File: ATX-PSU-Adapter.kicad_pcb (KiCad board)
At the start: 2 copper layers, 65 x 45 mm, 13 parts, among them J1 Conn_02x12_Top_Bottom, J2 Conn_01x06, J3 Conn_01x06, J4 Conn_01x06, J5 Conn_01x06, J6 Conn_01x06, J7 Conn_02x03_Odd_Even, U1 PC817

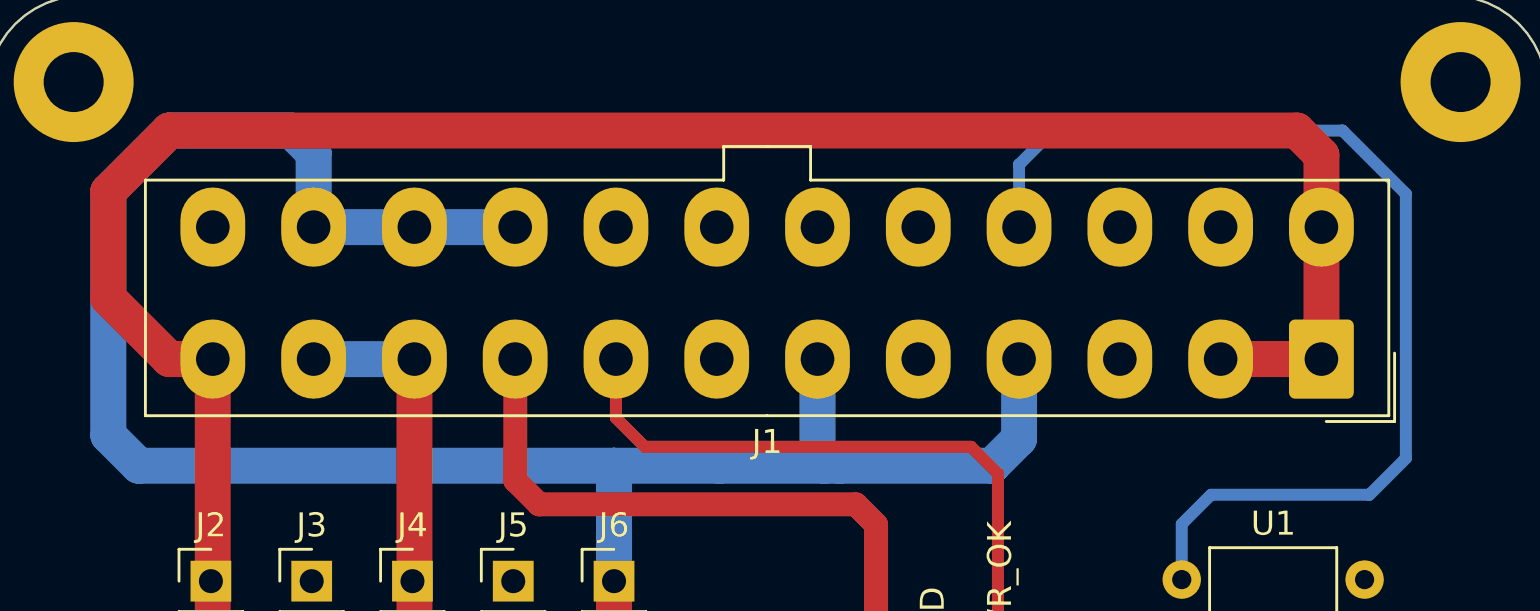
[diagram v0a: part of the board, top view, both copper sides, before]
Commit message: Replace ATX Connector
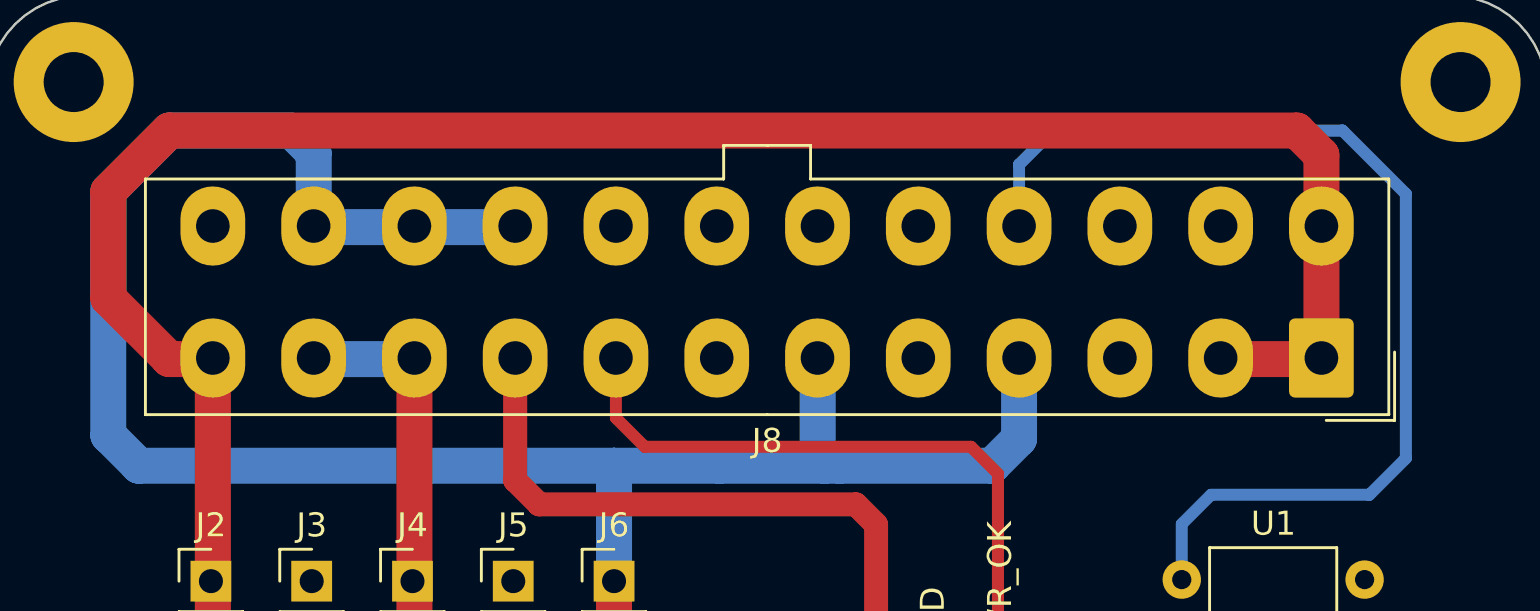
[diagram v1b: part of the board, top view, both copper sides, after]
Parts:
- removed J1: Conn_02x12_Top_Bottom, Connector_Molex:Molex_Mini-Fit_Jr_5566-24A_2x12_P4.20mm_Vertical
- added J8: ATX-24, Connector_Molex:Molex_Mini-Fit_Jr_5566-24A_2x12_P4.20mm_Vertical, F.Cu at (80.6, 40.1)
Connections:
- net +12V renamed /12V
- net +3.3V renamed /3.3V
- net +5P renamed /5VSB
- net +5V renamed /5V
- net /RPI-PS-ON renamed Net-(J7-Pin_5)
- J7 pad 6: /PG -> /PWR_OK
- U1 pad 3: /PS-ON -> /PS_ON
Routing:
- net /PS_ON: track 0.00 -> 44.2 mm
- net /PS-ON: track 44.2 -> 0.00 mm
- net /PWR_OK: track 0.00 -> 29.0 mm
- net /PG: track 29.0 -> 0.00 mm

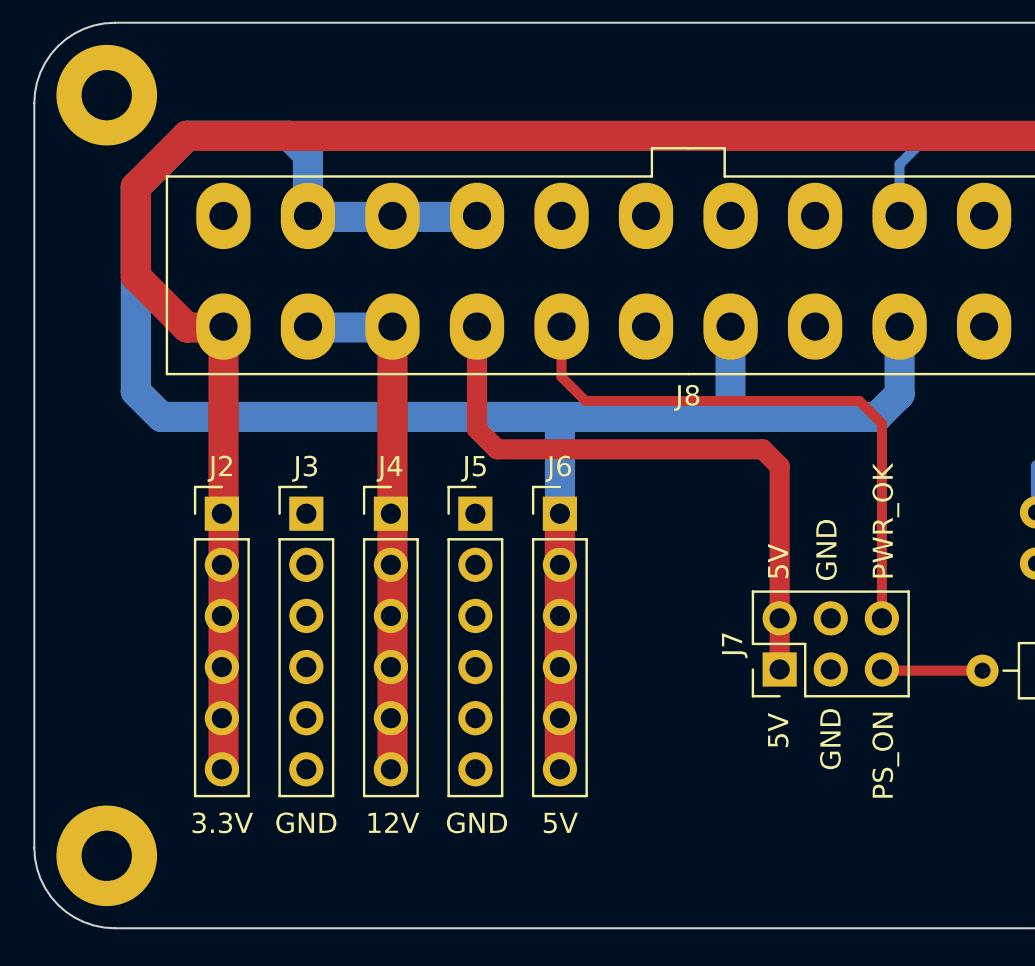
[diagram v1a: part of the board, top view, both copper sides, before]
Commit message: Replace pinheader
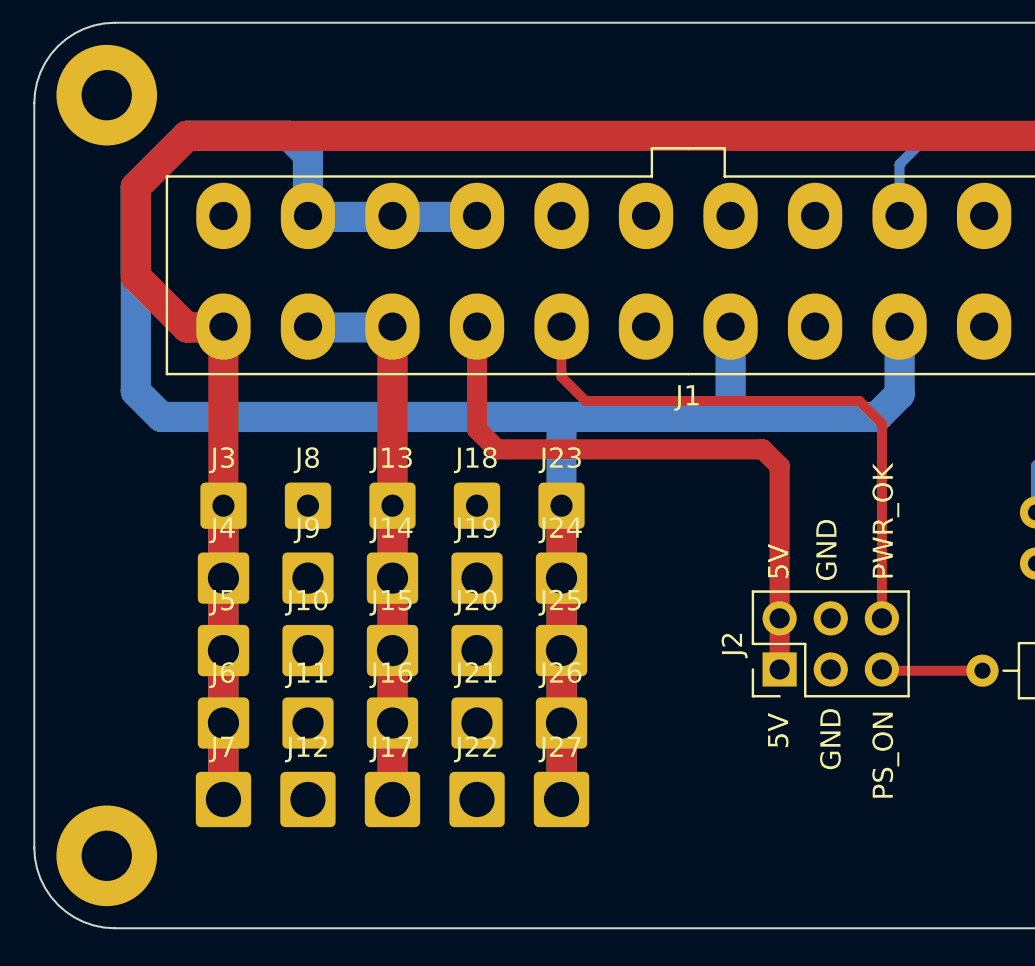
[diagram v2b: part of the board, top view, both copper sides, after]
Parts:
- removed the J2 at (34.3, 49.4)
- added J10: Conn_01x01, Connector_Wire:SolderWire-0.75sqmm_1x01_D1.25mm_OD2.3mm, F.Cu at (38.6, 56.2)
- added J11: Conn_01x01, Connector_Wire:SolderWire-0.75sqmm_1x01_D1.25mm_OD2.3mm, F.Cu at (38.6, 59.8)
- added J12: Conn_01x01, Connector_Wire:SolderWire-1sqmm_1x01_D1.4mm_OD2.7mm, F.Cu at (38.6, 63.6)
- added J13: Conn_01x01, Connector_Wire:SolderWire-0.5sqmm_1x01_D0.9mm_OD2.3mm, F.Cu at (42.8, 49.0)
- added J14: Conn_01x01, Connector_Wire:SolderWire-0.75sqmm_1x01_D1.25mm_OD2.3mm, F.Cu at (42.8, 52.6)
- added J15: Conn_01x01, Connector_Wire:SolderWire-0.75sqmm_1x01_D1.25mm_OD2.3mm, F.Cu at (42.8, 56.2)
- added J16: Conn_01x01, Connector_Wire:SolderWire-0.75sqmm_1x01_D1.25mm_OD2.3mm, F.Cu at (42.8, 59.8)
- added J17: Conn_01x01, Connector_Wire:SolderWire-1sqmm_1x01_D1.4mm_OD2.7mm, F.Cu at (42.8, 63.6)
- added J18: Conn_01x01, Connector_Wire:SolderWire-0.5sqmm_1x01_D0.9mm_OD2.3mm, F.Cu at (47.0, 49.0)
- added J19: Conn_01x01, Connector_Wire:SolderWire-0.75sqmm_1x01_D1.25mm_OD2.3mm, F.Cu at (47.0, 52.6)
- added J20: Conn_01x01, Connector_Wire:SolderWire-0.75sqmm_1x01_D1.25mm_OD2.3mm, F.Cu at (47.0, 56.2)
- added J21: Conn_01x01, Connector_Wire:SolderWire-0.75sqmm_1x01_D1.25mm_OD2.3mm, F.Cu at (47.0, 59.8)
- added J22: Conn_01x01, Connector_Wire:SolderWire-1sqmm_1x01_D1.4mm_OD2.7mm, F.Cu at (47.0, 63.6)
- added J23: Conn_01x01, Connector_Wire:SolderWire-0.5sqmm_1x01_D0.9mm_OD2.3mm, F.Cu at (51.2, 49.0)
- added J24: Conn_01x01, Connector_Wire:SolderWire-0.75sqmm_1x01_D1.25mm_OD2.3mm, F.Cu at (51.2, 52.6)
- added J25: Conn_01x01, Connector_Wire:SolderWire-0.75sqmm_1x01_D1.25mm_OD2.3mm, F.Cu at (51.2, 56.2)
- added J26: Conn_01x01, Connector_Wire:SolderWire-0.75sqmm_1x01_D1.25mm_OD2.3mm, F.Cu at (51.2, 59.8)
- added J27: Conn_01x01, Connector_Wire:SolderWire-1sqmm_1x01_D1.4mm_OD2.7mm, F.Cu at (51.2, 63.6)
- added J7: Conn_01x01, Connector_Wire:SolderWire-1sqmm_1x01_D1.4mm_OD2.7mm, F.Cu at (34.4, 63.6)
- added J8: Conn_01x01, Connector_Wire:SolderWire-0.5sqmm_1x01_D0.9mm_OD2.3mm, F.Cu at (38.6, 49.0)
- added J9: Conn_01x01, Connector_Wire:SolderWire-0.75sqmm_1x01_D1.25mm_OD2.3mm, F.Cu at (38.6, 52.6)
- J3: value Conn_01x06 -> Conn_01x01; footprint Connector_PinHeader_2.54mm:PinHeader_1x06_P2.54mm_Vertical -> Connector_Wire:SolderWire-0.5sqmm_1x01_D0.9mm_OD2.3mm
- J4, J5, J6: value Conn_01x06 -> Conn_01x01; footprint Connector_PinHeader_2.54mm:PinHeader_1x06_P2.54mm_Vertical -> Connector_Wire:SolderWire-0.75sqmm_1x01_D1.25mm_OD2.3mm
- moved J6 19.7 mm to (34.4, 59.8)
- moved J5 14.2 mm to (34.4, 56.2)
- moved J4 8.91 mm to (34.4, 52.6)
- moved J3 4.14 mm to (34.4, 49.0)
- renumbered J8 to J1, J7 to J2
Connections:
- J3 pad 1: GND -> /3.3V
- J4 pad 1: /12V -> /3.3V
- J5 pad 1: GND -> /3.3V
- J6 pad 1: /5V -> /3.3V
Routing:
- net /5V: track 96.0 -> 112.1 mm
- net /3.3V: track 96.6 -> 112.7 mm
- net /12V: track 26.2 -> 42.3 mm

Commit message: Adjust text
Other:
- board text added: "12V"
- board text added: "3.3V"
- board text added: "5V"
- board text added: "GND"
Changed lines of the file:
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@@
     (property "ki_keywords" "connector")
     (attr exclude_from_pos_files)
-    (fp_text reference "J3" (at 0 -2.35) (layer "F.SilkS")
+    (fp_text reference "J3" (at 0 -2.35) (layer "F.SilkS") hide
         (effects (font (size 1 1) (thickness 0.15)))
     )
@@
     (property "ki_keywords" "connector")
     (attr exclude_from_pos_files)
-    (fp_text reference "J23" (at 0 -2.35) (layer "F.SilkS")
+    (fp_text reference "J23" (at 0 -2.35) (layer "F.SilkS") hide
         (effects (font (size 1 1) (thickness 0.15)))
     )
@@
     (property "ki_keywords" "connector")
     (attr exclude_from_pos_files)
-    (fp_text reference "J22" (at 0 -2.58) (layer "F.SilkS")
+    (fp_text reference "J22" (at 0 -2.58) (layer "F.SilkS") hide
         (effects (font (size 1 1) (thickness 0.15)))
     )
@@
     (property "ki_keywords" "ATX PSU")
     (attr through_hole)
-    (fp_text reference "J1" (at 23.1 -3.45) (layer "F.SilkS")
+    (fp_text reference "J1" (at 23.1 10.1) (layer "F.SilkS")
         (effects (font (size 1 1) (thickness 0.15)))
     )
@@
     (property "ki_keywords" "connector")
     (attr exclude_from_pos_files)
-    (fp_text reference "J16" (at 0 -2.47) (layer "F.SilkS")
+    (fp_text reference "J16" (at 0 -2.47) (layer "F.SilkS") hide
         (effects (font (size 1 1) (thickness 0.15)))
     )
@@
     (property "ki_keywords" "connector")
     (attr exclude_from_pos_files)
-    (fp_text reference "J12" (at 0 -2.58) (layer "F.SilkS")
+    (fp_text reference "J12" (at 0 -2.58) (layer "F.SilkS") hide
         (effects (font (size 1 1) (thickness 0.15)))
     )
@@
     (property "ki_keywords" "connector")
     (attr exclude_from_pos_files)
-    (fp_text reference "J25" (at 0 -2.47) (layer "F.SilkS")
+    (fp_text reference "J25" (at 0 -2.47) (layer "F.SilkS") hide
         (effects (font (size 1 1) (thickness 0.15)))
     )
@@
     (property "ki_keywords" "connector")
     (attr exclude_from_pos_files)
-    (fp_text reference "J20" (at 0 -2.47) (layer "F.SilkS")
+    (fp_text reference "J20" (at 0 -2.47) (layer "F.SilkS") hide
         (effects (font (size 1 1) (thickness 0.15)))
     )
@@
     (property "ki_keywords" "connector")
     (attr exclude_from_pos_files)
-    (fp_text reference "J10" (at 0 -2.47) (layer "F.SilkS")
+    (fp_text reference "J10" (at 0 -2.47) (layer "F.SilkS") hide
         (effects (font (size 1 1) (thickness 0.15)))
     )
@@
     (property "ki_keywords" "connector")
     (attr exclude_from_pos_files)
-    (fp_text reference "J14" (at 0 -2.47) (layer "F.SilkS")
+    (fp_text reference "J14" (at 0 -2.47) (layer "F.SilkS") hide
         (effects (font (size 1 1) (thickness 0.15)))
     )
@@
     (property "ki_keywords" "connector")
     (attr exclude_from_pos_files)
-    (fp_text reference "J19" (at 0 -2.47) (layer "F.SilkS")
+    (fp_text reference "J19" (at 0 -2.47) (layer "F.SilkS") hide
         (effects (font (size 1 1) (thickness 0.15)))
     )
@@
     (property "ki_keywords" "connector")
     (attr exclude_from_pos_files)
-    (fp_text reference "J13" (at 0 -2.35) (layer "F.SilkS")
+    (fp_text reference "J13" (at 0 -2.35) (layer "F.SilkS") hide
         (effects (font (size 1 1) (thickness 0.15)))
     )
@@
     (property "ki_keywords" "connector")
     (attr exclude_from_pos_files)
-    (fp_text reference "J27" (at 0 -2.58) (layer "F.SilkS")
+    (fp_text reference "J27" (at 0 -2.58) (layer "F.SilkS") hide
         (effects (font (size 1 1) (thickness 0.15)))
     )
@@
     (property "ki_keywords" "connector")
     (attr exclude_from_pos_files)
-    (fp_text reference "J5" (at 0 -2.47) (layer "F.SilkS")
+    (fp_text reference "J5" (at 0 -2.47) (layer "F.SilkS") hide
         (effects (font (size 1 1) (thickness 0.15)))
     )
@@
     (property "ki_keywords" "mounting hole")
     (attr exclude_from_pos_files)
-    (fp_text reference "H1" (at 4.2 0) (layer "F.Fab")
+    (fp_text reference "H1" (at 4.2 0) (layer "F.SilkS") hide
         (effects (font (size 1 1) (thickness 0.15)))
     )
@@
     (property "ki_keywords" "connector")
     (attr exclude_from_pos_files)
-    (fp_text reference "J4" (at 0 -2.47) (layer "F.SilkS")
+    (fp_text reference "J4" (at 0 -2.47) (layer "F.SilkS") hide
         (effects (font (size 1 1) (thickness 0.15)))
     )
@@
     (property "ki_keywords" "connector")
     (attr exclude_from_pos_files)
-    (fp_text reference "J17" (at 0 -2.58) (layer "F.SilkS")
+    (fp_text reference "J17" (at 0 -2.58) (layer "F.SilkS") hide
         (effects (font (size 1 1) (thickness 0.15)))
     )
@@
     (property "ki_keywords" "mounting hole")
     (attr exclude_from_pos_files)
-    (fp_text reference "H2" (at -4.4 0) (layer "F.Fab")
+    (fp_text reference "H2" (at -4.4 0) (layer "F.SilkS") hide
         (effects (font (size 1 1) (thickness 0.15)))
     )
@@
     (property "ki_keywords" "connector")
     (attr exclude_from_pos_files)
-    (fp_text reference "J9" (at 0 -2.47) (layer "F.SilkS")
+    (fp_text reference "J9" (at 0 -2.47) (layer "F.SilkS") hide
         (effects (font (size 1 1) (thickness 0.15)))
     )
@@
     (property "ki_keywords" "connector")
     (attr exclude_from_pos_files)
-    (fp_text reference "J11" (at 0 -2.47) (layer "F.SilkS")
+    (fp_text reference "J11" (at 0 -2.47) (layer "F.SilkS") hide
         (effects (font (size 1 1) (thickness 0.15)))
     )
@@
     (property "ki_keywords" "connector")
     (attr exclude_from_pos_files)
-    (fp_text reference "J7" (at 0 -2.58) (layer "F.SilkS")
+    (fp_text reference "J7" (at 0 -2.58) (layer "F.SilkS") hide
         (effects (font (size 1 1) (thickness 0.15)))
     )
@@
     (property "ki_keywords" "connector")
     (attr exclude_from_pos_files)
-    (fp_text reference "J8" (at 0 -2.35) (layer "F.SilkS")
+    (fp_text reference "J8" (at 0 -2.35) (layer "F.SilkS") hide
         (effects (font (size 1 1) (thickness 0.15)))
     )
@@
     (property "ki_keywords" "connector")
     (attr exclude_from_pos_files)
-    (fp_text reference "J6" (at 0 -2.47) (layer "F.SilkS")
+    (fp_text reference "J6" (at 0 -2.47) (layer "F.SilkS") hide
         (effects (font (size 1 1) (thickness 0.15)))
     )
@@
     (property "ki_keywords" "mounting hole")
     (attr exclude_from_pos_files)
-    (fp_text reference "H4" (at 4.2 0) (layer "F.Fab")
+    (fp_text reference "H4" (at 4.2 0) (layer "F.SilkS") hide
         (effects (font (size 1 1) (thickness 0.15)))
     )
@@
     (property "ki_keywords" "connector")
     (attr exclude_from_pos_files)
-    (fp_text reference "J21" (at 0 -2.47) (layer "F.SilkS")
+    (fp_text reference "J21" (at 0 -2.47) (layer "F.SilkS") hide
         (effects (font (size 1 1) (thickness 0.15)))
     )
@@
     (property "ki_keywords" "connector")
     (attr exclude_from_pos_files)
-    (fp_text reference "J15" (at 0 -2.47) (layer "F.SilkS")
+    (fp_text reference "J15" (at 0 -2.47) (layer "F.SilkS") hide
         (effects (font (size 1 1) (thickness 0.15)))
     )
@@
     (property "ki_keywords" "connector")
     (attr exclude_from_pos_files)
-    (fp_text reference "J24" (at 0 -2.47) (layer "F.SilkS")
+    (fp_text reference "J24" (at 0 -2.47) (layer "F.SilkS") hide
         (effects (font (size 1 1) (thickness 0.15)))
     )
@@
     (property "ki_keywords" "connector")
     (attr exclude_from_pos_files)
-    (fp_text reference "J18" (at 0 -2.35) (layer "F.SilkS")
+    (fp_text reference "J18" (at 0 -2.35) (layer "F.SilkS") hide
         (effects (font (size 1 1) (thickness 0.15)))
     )
@@
     (property "ki_keywords" "connector")
     (attr exclude_from_pos_files)
-    (fp_text reference "J26" (at 0 -2.47) (layer "F.SilkS")
+    (fp_text reference "J26" (at 0 -2.47) (layer "F.SilkS") hide
         (effects (font (size 1 1) (thickness 0.15)))
     )
@@
     (property "ki_keywords" "mounting hole")
     (attr exclude_from_pos_files)
-    (fp_text reference "H3" (at -4.4 0) (layer "F.Fab")
+    (fp_text reference "H3" (at -4.4 0) (layer "F.SilkS") hide
         (effects (font (size 1 1) (thickness 0.15)))
     )
@@
   (gr_line (start 86 25) (end 29 25)
     (stroke (width 0.1) (type default)) (layer "Edge.Cuts"))
-  (gr_text "JLCJLCJLCJLC" (at 57.5 66.4) (layer "B.SilkS")
+  (gr_text "JLCJLCJLCJLC" (at 57.6 29.2) (layer "B.SilkS")
     (effects (font (size 1 1) (thickness 0.15)) (justify bottom mirror))
   )
+  (gr_text "GND" (at 40.2 67) (layer "B.SilkS")
+    (effects (font (size 1 1) (thickness 0.15)) (justify left bottom mirror))
+  )
+  (gr_text "5V" (at 52.2 67) (layer "B.SilkS")
+    (effects (font (size 1 1) (thickness 0.15)) (justify left bottom mirror))
+  )
+  (gr_text "3.3V" (at 36 67) (layer "B.SilkS")
+    (effects (font (size 1 1) (thickness 0.15)) (justify left bottom mirror))
+  )
+  (gr_text "GND" (at 48.6 67) (layer "B.SilkS")
+    (effects (font (size 1 1) (thickness 0.15)) (justify left bottom mirror))
+  )
+  (gr_text "12V" (at 44.2 67) (layer "B.SilkS")
+    (effects (font (size 1 1) (thickness 0.15)) (justify left bottom mirror))
+  )
+  (gr_text "3.3V" (at 32.6 67) (layer "F.SilkS")
+    (effects (font (size 1 1) (thickness 0.15)) (justify left bottom))
+  )
+  (gr_text "12V" (at 41.2 67) (layer "F.SilkS")
+    (effects (font (size 1 1) (thickness 0.15)) (justify left bottom))
+  )
+  (gr_text "5V" (at 50.2 67) (layer "F.SilkS")
+    (effects (font (size 1 1) (thickness 0.15)) (justify left bottom))
+  )
+  (gr_text "GND" (at 37 67) (layer "F.SilkS")
+    (effects (font (size 1 1) (thickness 0.15)) (justify left bottom))
+  )
+  (gr_text "GND" (at 45.4 67) (layer "F.SilkS")
+    (effects (font (size 1 1) (thickness 0.15)) (justify left bottom))
+  )
   (segment (start 34.4 40.1) (end 34.4 63.6) (width 1.5) (layer "F.Cu") (net 2))
